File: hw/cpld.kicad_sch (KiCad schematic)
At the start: 32 parts, among them U1401 ICE40LP1K-QN84, Y1401 Si5351C-B-GM, Y1402 40MHz

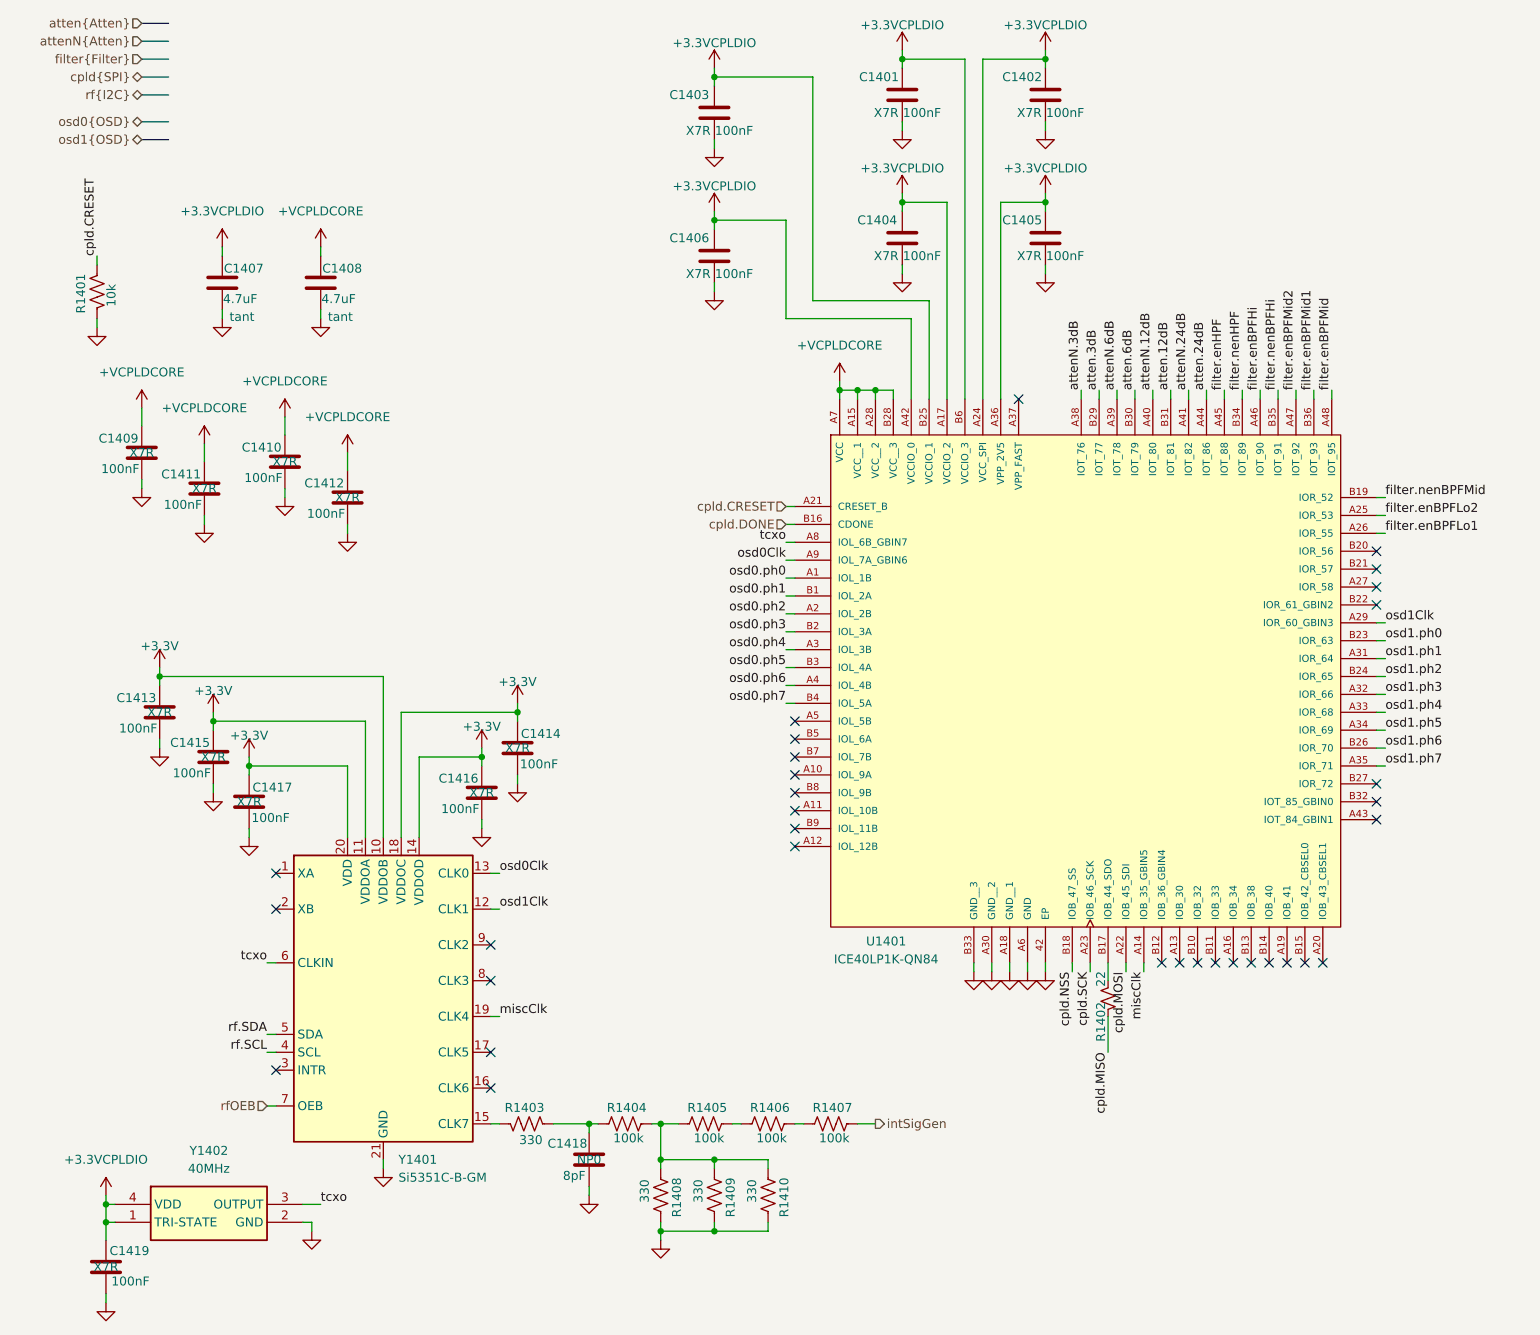
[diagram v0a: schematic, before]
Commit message: Now two CPLDs, new placement for better routing of clocks and symmetry for delay. Not routed yet but placement is "complete".
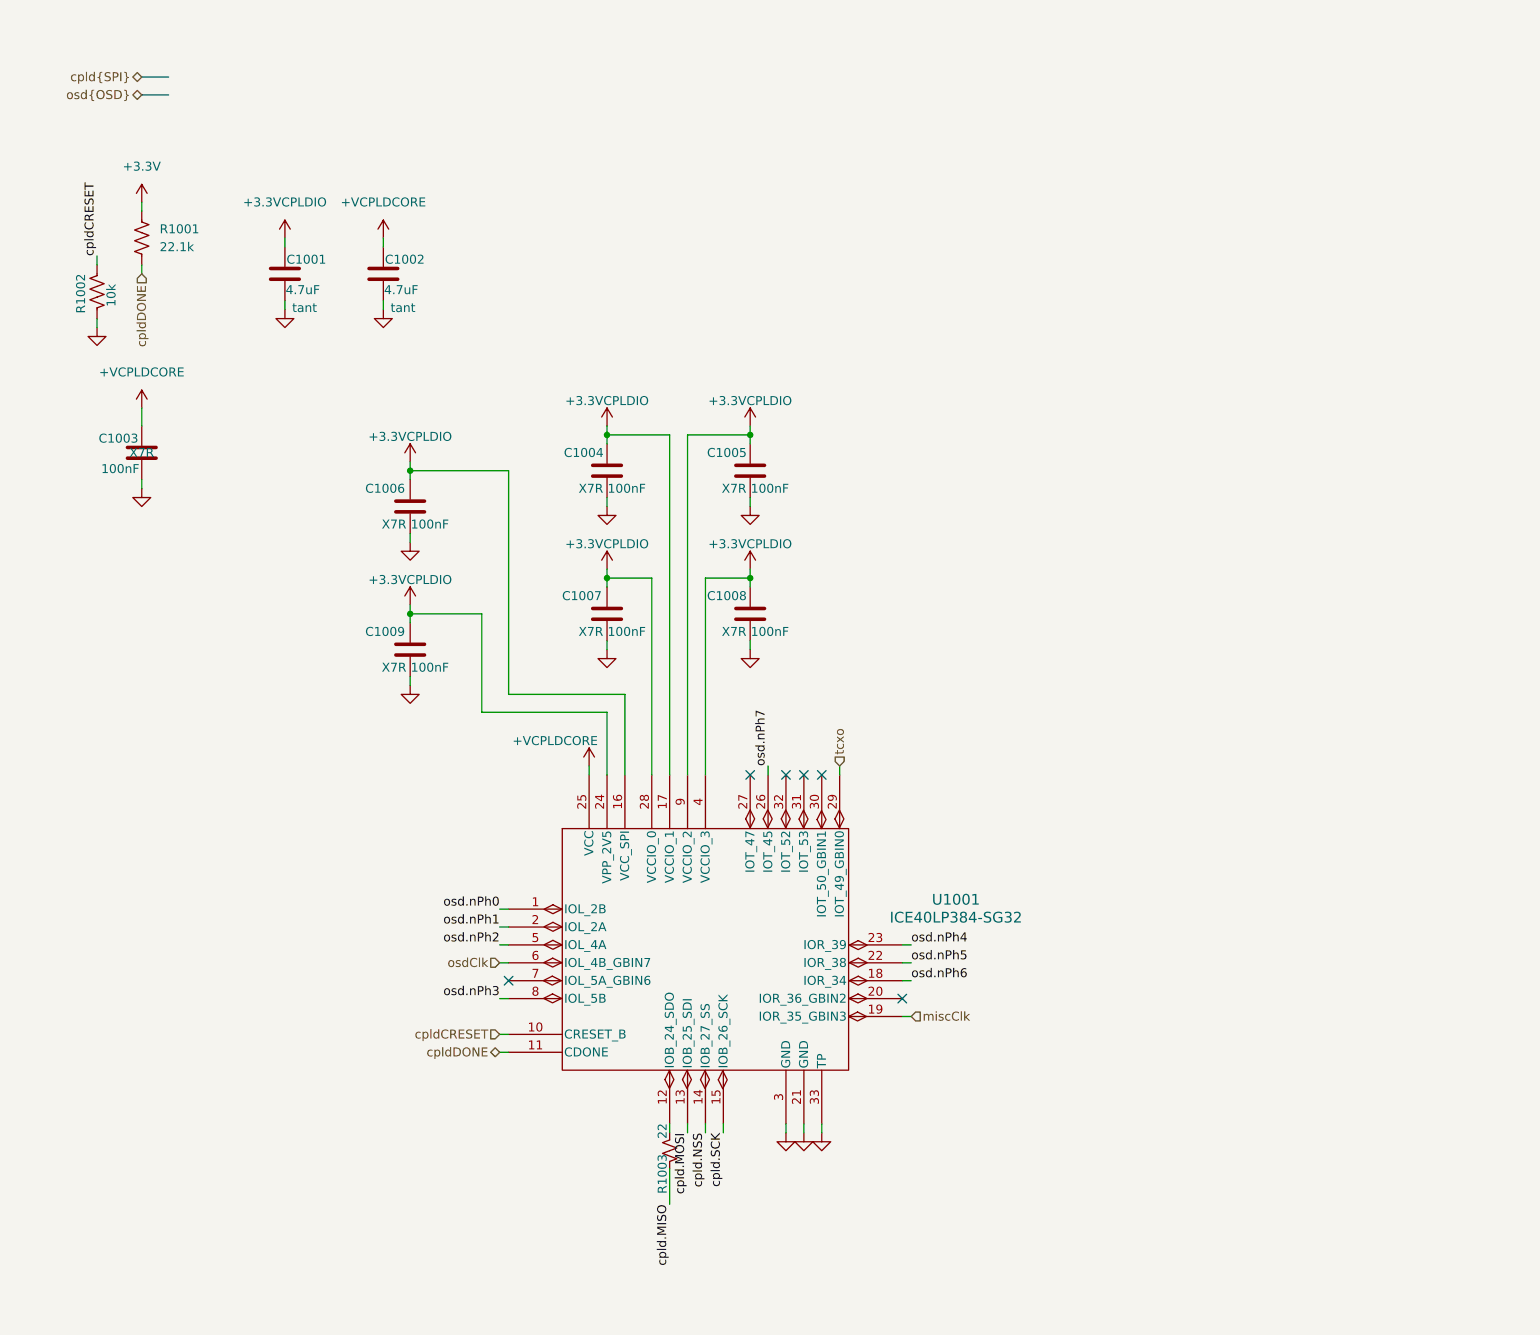
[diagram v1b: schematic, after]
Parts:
- removed C1410, C1411, C1412, C1413, C1414, C1415, C1416, C1417, C1419: 100nF, Capacitor_SMD:C_0402_1005Metric, symbol Device:C
- removed C1418: 8pF, Capacitor_SMD:C_0603_1608Metric, symbol Device:C
- removed R1403, R1408, R1409, R1410: 330, Resistor_SMD:R_0402_1005Metric, symbol Device:R_US
- removed R1404, R1405, R1406, R1407: 100k, Resistor_SMD:R_0402_1005Metric, symbol Device:R_US
- removed U1401: ICE40LP1K-QN84, Library:LATTICE_ICE40LP1K-QN84, symbol Library:ICE40LP1K-QN84
- removed Y1401: Si5351C-B-GM, Package_DFN_QFN:QFN-20-1EP_4x4mm_P0.5mm_EP2.7x2.7mm, symbol Oscillator:Si5351C-B-GM
- removed Y1402: 40MHz, Library:ECSTXO201633400TR, symbol Library:ECS-TXO-2016-33-400-TR
- added R1001: 22.1k, Resistor_SMD:R_0402_1005Metric, symbol Device:R_US
- added U1001: ICE40LP384-SG32, Library:QFNS32_LAT, symbol Library:ICE40LP384-SG32
- renumbered C1407 to C1001, C1408 to C1002, C1409 to C1003, C1401 to C1004, C1402 to C1005, C1403 to C1006, C1404 to C1007, C1405 to C1008, C1406 to C1009, R1401 to R1002, R1402 to R1003
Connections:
- net +3.3V: now also R1001.1
- net +3.3VCPLDIO: now also U1001.16 (VCC_SPI), U1001.17 (VCCIO_1), U1001.24 (VPP_2V5), U1001.28 (VCCIO_0), U1001.4 (VCCIO_3), U1001.9 (VCCIO_2)
- net +VCPLDCORE: now also U1001.25 (VCC)
- net GND: now also U1001.21 (GND), U1001.3 (GND), U1001.33 (TP)
- net cpld.MOSI: now also U1001.13 (IOB_25_SDI)
- net cpld.NSS: now also U1001.14 (IOB_27_SS)
- net cpld.SCK: now also U1001.15 (IOB_26_SCK)
- net miscClk: now also U1001.19 (IOR_35_GBIN3)
- net tcxo: now also U1001.29 (IOT_49_GBIN0)
- net at R1003.1: now also U1001.12 (IOB_24_SDO)
- net cpld.CRESET renamed cpldCRESET
- net cpldCRESET: now also U1001.10 (CRESET_B)
- new net cpldDONE: R1001.2, U1001.11 (CDONE)
- new net osd.nPh0: U1001.1 (IOL_2B)
- new net osd.nPh1: U1001.2 (IOL_2A)
- new net osd.nPh2: U1001.5 (IOL_4A)
- new net osd.nPh3: U1001.8 (IOL_5B)
- new net osd.nPh4: U1001.23 (IOR_39)
- new net osd.nPh5: U1001.22 (IOR_38)
- new net osd.nPh6: U1001.18 (IOR_34)
- new net osd.nPh7: U1001.26 (IOT_45)
- new net osdClk: U1001.6 (IOL_4B_GBIN7)
- no-connect marks 33 -> 6
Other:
- moved on the sheet: C1001, C1002, C1004, C1005, C1006, C1007, C1008, C1009, R1003

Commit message: Route some clocks. Not done yet.
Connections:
- net osdClk: now also U1001.20 (IOR_36_GBIN2); no longer U1001.6 (IOL_4B_GBIN7)
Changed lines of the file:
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@@
+	)
+	(no_connect
+		(at 78.74 148.59)
 	)
 	(no_connect
@@
 	)
 	(no_connect
-		(at 134.62 153.67)
-	)
-	(no_connect
 		(at 78.74 151.13)
 	)
@@
 	(wire
 		(pts
-			(xy 77.47 148.59) (xy 78.74 148.59)
-		)
-		(stroke
-			(width 0)
-			(type default)
-		)
-	)
-	(wire
-		(pts
 			(xy 90.17 120.65) (xy 90.17 121.92)
 		)
@@
 		(pts
 			(xy 113.03 93.98) (xy 113.03 95.25)
+		)
+		(stroke
+			(width 0)
+			(type default)
+		)
+	)
+	(wire
+		(pts
+			(xy 134.62 153.67) (xy 135.89 153.67)
 		)
 		(stroke
@@
 	(hierarchical_label "osdClk"
 		(shape input)
-		(at 77.47 148.59 180)
-		(effects
-			(font
-				(size 1.27 1.27)
-			)
-			(justify right)
-		)
-	)
+		(at 135.89 153.67 0)
+		(effects
+			(font
+				(size 1.27 1.27)
+			)
+			(justify left)
+		)
+	)

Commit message: Checkpoint before replicating OSD and then CPLD layout from 0 to 1
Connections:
- net miscClk: now also U1001.30 (IOT_50_GBIN1); no longer U1001.19 (IOR_35_GBIN3)
- net osd.nPh1: now also U1001.5 (IOL_4A); no longer U1001.2 (IOL_2A)
- net osd.nPh2: now also U1001.8 (IOL_5B); no longer U1001.5 (IOL_4A)
- net osd.nPh3: now also U1001.2 (IOL_2A); no longer U1001.8 (IOL_5B)
- net osd.nPh4: now also U1001.18 (IOR_34); no longer U1001.23 (IOR_39)
- net osd.nPh6: now also U1001.23 (IOR_39); no longer U1001.18 (IOR_34)
- net osd.nPh7: now also U1001.19 (IOR_35_GBIN3); no longer U1001.26 (IOT_45)
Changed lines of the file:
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@@
-	)
-	(no_connect
-		(at 123.19 121.92)
 	)
 	(no_connect
@@
 	)
 	(no_connect
+		(at 115.57 121.92)
+	)
+	(no_connect
 		(at 120.65 121.92)
 	)
@@
 	(wire
 		(pts
-			(xy 115.57 120.65) (xy 115.57 121.92)
+			(xy 135.89 156.21) (xy 134.62 156.21)
 		)
 		(stroke
@@
 	(wire
 		(pts
-			(xy 135.89 156.21) (xy 134.62 156.21)
+			(xy 123.19 120.65) (xy 123.19 121.92)
 		)
 		(stroke
@@
 	)
 	(label "osd.nPh4"
-		(at 135.89 146.05 0)
+		(at 135.89 151.13 0)
 		(effects
 			(font
@@
 	)
 	(label "osd.nPh2"
-		(at 77.47 146.05 180)
+		(at 77.47 153.67 180)
 		(effects
 			(font
@@
 	)
 	(label "osd.nPh3"
-		(at 77.47 153.67 180)
+		(at 77.47 143.51 180)
 		(effects
 			(font
@@
 	)
 	(label "osd.nPh7"
-		(at 115.57 120.65 90)
+		(at 135.89 156.21 0)
 		(effects
 			(font
@@
 	)
 	(label "osd.nPh1"
-		(at 77.47 143.51 180)
+		(at 77.47 146.05 180)
 		(effects
 			(font
@@
 	)
 	(label "osd.nPh6"
-		(at 135.89 151.13 0)
+		(at 135.89 146.05 0)
 		(effects
 			(font
@@
 	(hierarchical_label "miscClk"
 		(shape input)
-		(at 135.89 156.21 0)
-		(effects
-			(font
+		(at 123.19 120.65 90)
+		(effects
+			(font

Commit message: PCB and schematic both pass DRC and all nets routed. Now for some desk checking...
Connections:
- net miscClk: no longer names the net of U1001.30 (IOT_50_GBIN1)
- no-connect marks 6 -> 7
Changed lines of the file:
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@@
+	)
+	(no_connect
+		(at 123.19 121.92)
 	)
 	(no_connect
@@
 		(pts
 			(xy 26.67 40.64) (xy 26.67 41.91)
-		)
-		(stroke
-			(width 0)
-			(type default)
-		)
-	)
-	(wire
-		(pts
-			(xy 123.19 120.65) (xy 123.19 121.92)
 		)
 		(stroke
@@
 		(effects
 			(font
-				(size 1.27 1.27)
-			)
-			(justify left)
-		)
-	)
-	(hierarchical_label "miscClk"
-		(shape input)
-		(at 123.19 120.65 90)
-		(effects
-			(font

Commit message: 3D rendering now. All DRCs pass on schematic and PCB. BOM scrubbed to coallesce parts. Still no part numbers for most.
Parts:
- C1001, C1002: footprint Capacitor_SMD:C_0805_2012Metric -> Capacitor_SMD:C_0402_1005Metric; cap-type tant -> X7R; working-voltage 10V -> 25V
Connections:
- net gnssPPS: now reaches U1001.32 (IOT_52)
- no-connect marks 7 -> 6
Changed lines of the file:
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@@
 	)
 	(no_connect
-		(at 118.11 121.92)
-	)
-	(no_connect
 		(at 115.57 121.92)
 	)
@@
 		)
 	)
+	(wire
+		(pts
+			(xy 118.11 120.65) (xy 118.11 121.92)
+		)
+		(stroke
+			(width 0)
+			(type default)
+		)
+	)
 	(label "osd.nPh0"
 		(at 77.47 140.97 180)
@@
 		)
 	)
+	(hierarchical_label "gnssPPS"
+		(shape input)
+		(at 118.11 120.65 90)
+		(effects
+			(font
+				(size 1.27 1.27)
+			)
+			(justify left)
+		)
+	)
 	(hierarchical_label "cpldDONE"
 		(shape input)
@@
 			)
 		)
-		(property "Footprint" "Capacitor_SMD:C_0805_2012Metric"
+		(property "Footprint" "Capacitor_SMD:C_0402_1005Metric"
 			(at 47.9552 54.61 0)
 			(effects
@@
 			)
 		)
-		(property "cap-type" "tant"
+		(property "cap-type" "X7R"
 			(at 49.784 55.626 0)
 			(effects
@@
 			)
 		)
-		(property "working-voltage" "10V"
+		(property "working-voltage" "25V"
 			(at 46.99 50.8 0)
 			(effects
@@
 			)
 		)
-		(property "Footprint" "Capacitor_SMD:C_0805_2012Metric"
+		(property "Footprint" "Capacitor_SMD:C_0402_1005Metric"
 			(at 61.9252 54.61 0)
 			(effects
@@
 			)
 		)
-		(property "cap-type" "tant"
+		(property "cap-type" "X7R"
 			(at 63.754 55.626 0)
 			(effects
@@
 			)
 		)
-		(property "working-voltage" "10V"
+		(property "working-voltage" "25V"
 			(at 60.96 50.8 0)
 			(effects

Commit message: Set up for DVT2 PCBA build at JLCPCB
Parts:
- C1001, C1002: MPN 298D475X9010M2T -> (none)
- C1003, C1004, C1005, C1006, C1007, C1008, C1009: MPN C0805F104K1RACAUTO -> (none)
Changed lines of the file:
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@@
 			)
 		)
-		(property "MPN" "C0805F104K1RACAUTO"
+		(property "MPN" ""
 			(at -48.26 50.8 0)
 			(effects
@@
 			)
 		)
-		(property "MPN" "C0805F104K1RACAUTO"
+		(property "MPN" ""
 			(at -76.2 55.88 0)
 			(effects
@@
 			)
 		)
-		(property "MPN" "C0805F104K1RACAUTO"
+		(property "MPN" ""
 			(at -154.94 -20.32 0)
 			(effects
@@
 			)
 		)
-		(property "MPN" "C0805F104K1RACAUTO"
+		(property "MPN" ""
 			(at -76.2 35.56 0)
 			(effects
@@
 			)
 		)
-		(property "MPN" "298D475X9010M2T"
+		(property "MPN" ""
 			(at 19.05 7.62 0)
 			(effects
@@
 			)
 		)
-		(property "MPN" "C0805F104K1RACAUTO"
+		(property "MPN" ""
 			(at -93.98 62.23 0)
 			(effects
@@
 			)
 		)
-		(property "MPN" "C0805F104K1RACAUTO"
+		(property "MPN" ""
 			(at -48.26 30.48 0)
 			(effects
@@
 			)
 		)
-		(property "MPN" "298D475X9010M2T"
+		(property "MPN" ""
 			(at 19.05 7.62 0)
 			(effects
@@
 			)
 		)
-		(property "MPN" "C0805F104K1RACAUTO"
+		(property "MPN" ""
 			(at -93.98 41.91 0)
 			(effects

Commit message: Switch to parts I can source from Mouser
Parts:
- C1001, C1002: MFG (none) -> Kyocera; MPN (none) -> CM05X5R475M10AH; Mouser Part Number (none) -> 346-CM05X5R475M10AH; cap-type X7R -> X5R; working-voltage 25V -> 10V
- C1003, C1004, C1005, C1006, C1007, C1008, C1009: MFG (none) -> muRata; MPN (none) -> GCM155R71H104KE02D; Mouser Part Number (none) -> 81-GCM155R71H104KE2D
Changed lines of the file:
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@@
 			)
 		)
-		(property "MPN" ""
+		(property "MPN" "GCM155R71H104KE02D"
 			(at -48.26 50.8 0)
 			(effects
@@
 			)
 		)
+		(property "MFG" "muRata"
+			(at 92.71 99.06 0)
+			(effects
+				(font
+					(size 1.27 1.27)
+				)
+				(hide yes)
+			)
+		)
+		(property "Mouser Part Number" "81-GCM155R71H104KE2D"
+			(at 92.71 99.06 0)
+			(effects
+				(font
+					(size 1.27 1.27)
+				)
+				(hide yes)
+			)
+		)
 		(pin "2"
 		)
@@
 			)
 		)
-		(property "MPN" ""
+		(property "MPN" "GCM155R71H104KE02D"
 			(at -76.2 55.88 0)
 			(effects
@@
 			)
 		)
+		(property "MFG" "muRata"
+			(at 64.77 104.14 0)
+			(effects
+				(font
+					(size 1.27 1.27)
+				)
+				(hide yes)
+			)
+		)
+		(property "Mouser Part Number" "81-GCM155R71H104KE2D"
+			(at 64.77 104.14 0)
+			(effects
+				(font
+					(size 1.27 1.27)
+				)
+				(hide yes)
+			)
+		)
 		(pin "2"
 		)
@@
 			)
 		)
-		(property "MPN" ""
+		(property "MPN" "GCM155R71H104KE02D"
 			(at -154.94 -20.32 0)
 			(effects
@@
 			)
 		)
+		(property "MFG" "muRata"
+			(at 26.67 76.2 0)
+			(effects
+				(font
+					(size 1.27 1.27)
+				)
+				(hide yes)
+			)
+		)
+		(property "Mouser Part Number" "81-GCM155R71H104KE2D"
+			(at 26.67 76.2 0)
+			(effects
+				(font
+					(size 1.27 1.27)
+				)
+				(hide yes)
+			)
+		)
 		(pin "2"
 		)
@@
 			)
 		)
-		(property "MPN" ""
+		(property "MPN" "GCM155R71H104KE02D"
 			(at -76.2 35.56 0)
 			(effects
@@
 			)
 		)
+		(property "MFG" "muRata"
+			(at 64.77 83.82 0)
+			(effects
+				(font
+					(size 1.27 1.27)
+				)
+				(hide yes)
+			)
+		)
+		(property "Mouser Part Number" "81-GCM155R71H104KE2D"
+			(at 64.77 83.82 0)
+			(effects
+				(font
+					(size 1.27 1.27)
+				)
+				(hide yes)
+			)
+		)
 		(pin "2"
 		)
@@
 			)
 		)
-		(property "MPN" ""
+		(property "MPN" "CM05X5R475M10AH"
 			(at 19.05 7.62 0)
 			(effects
@@
 			)
 		)
-		(property "cap-type" "X7R"
+		(property "cap-type" "X5R"
 			(at 49.784 55.626 0)
 			(effects
@@
 			)
 		)
-		(property "working-voltage" "25V"
+		(property "working-voltage" "10V"
 			(at 46.99 50.8 0)
 			(effects
@@
 			)
 		)
+		(property "MFG" "Kyocera"
+			(at 46.99 50.8 0)
+			(effects
+				(font
+					(size 1.27 1.27)
+				)
+				(hide yes)
+			)
+		)
+		(property "Mouser Part Number" "346-CM05X5R475M10AH"
+			(at 46.99 50.8 0)
+			(effects
+				(font
+					(size 1.27 1.27)
+				)
+				(hide yes)
+			)
+		)
 		(pin "2"
 		)
@@
 			)
 		)
-		(property "MPN" ""
+		(property "MPN" "GCM155R71H104KE02D"
 			(at -93.98 62.23 0)
 			(effects
@@
 			)
 		)
+		(property "MFG" "muRata"
+			(at 113.03 99.06 0)
+			(effects
+				(font
+					(size 1.27 1.27)
+				)
+				(hide yes)
+			)
+		)
+		(property "Mouser Part Number" "81-GCM155R71H104KE2D"
+			(at 113.03 99.06 0)
+			(effects
+				(font
+					(size 1.27 1.27)
+				)
+				(hide yes)
+			)
+		)
 		(pin "2"
 		)
@@
 			)
 		)
-		(property "MPN" ""
+		(property "MPN" "GCM155R71H104KE02D"
 			(at -48.26 30.48 0)
 			(effects
@@
 			)
 		)
+		(property "MFG" "muRata"
+			(at 92.71 78.74 0)
+			(effects
+				(font
+					(size 1.27 1.27)
+				)
+				(hide yes)
+			)
+		)
+		(property "Mouser Part Number" "81-GCM155R71H104KE2D"
+			(at 92.71 78.74 0)
+			(effects
+				(font
+					(size 1.27 1.27)
+				)
+				(hide yes)
+			)
+		)
 		(pin "2"
 		)
@@
 			)
 		)
-		(property "MPN" ""
+		(property "MPN" "CM05X5R475M10AH"
 			(at 19.05 7.62 0)
 			(effects
@@
 			)
 		)
-		(property "cap-type" "X7R"
+		(property "cap-type" "X5R"
 			(at 63.754 55.626 0)
 			(effects
@@
 			)
 		)
-		(property "working-voltage" "25V"
+		(property "working-voltage" "10V"
 			(at 60.96 50.8 0)
 			(effects
@@
 			)
 		)
+		(property "MFG" "Kyocera"
+			(at 60.96 50.8 0)
+			(effects
+				(font
+					(size 1.27 1.27)
+				)
+				(hide yes)
+			)
+		)
+		(property "Mouser Part Number" "346-CM05X5R475M10AH"
+			(at 60.96 50.8 0)
+			(effects
+				(font
+					(size 1.27 1.27)
+				)
+				(hide yes)
+			)
+		)
 		(pin "2"
 		)
@@
 			)
 		)
-		(property "MPN" ""
+		(property "MPN" "GCM155R71H104KE02D"
 			(at -93.98 41.91 0)
 			(effects
@@
 			(at 113.03 78.74 0)
 			(effects
+				(font
+					(size 1.27 1.27)
+				)
+				(hide yes)
+			)
+		)
+		(property "MFG" "muRata"
+			(at 113.03 78.74 0)
+			(effects
+				(font
+					(size 1.27 1.27)
+				)
+				(hide yes)
+			)
+		)
+		(property "Mouser Part Number" "81-GCM155R71H104KE2D"
+			(at 113.03 78.74 0)
+			(effects
